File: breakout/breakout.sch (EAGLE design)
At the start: 140 parts, among them J15 1789472, J18 1789472, J29 69168-124HLF, J30 SJ1-3514-SMT-TR, J31 12226-8250-00FR, J32 1888276, J33 69168-116HLF, J34 1888276, J35 69168-116HLF, Q1 SI1012R, Q2 SI1012R, Q3 SI1012R, Q4 SI1012R, U1 G6K-2F-RF, U10 SN65LVDS9638DGN, U11 TINY-FPGA-BX, U2 G6K-2F-RF, U3 G6K-2F-RF, U4 G6K-2F-RF, U5 LTM4622A, U6 SI8610, U7 TCA9555, U8 FIN1032MTCX, U9 SN65LVDS9638DGN

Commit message: Added RGB LEDs and driver to breakout-board
- The old circuit, with single green LEDs driven by the TCA9555 is still
there and functional if this circuit is not populated
- If it is, the LED outputs on the TCA should be set to hiZ
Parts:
- removed D17, D18, D19, D20: (no value), jonnew:LED_3MM
- added C23: 0.1uF, jonnew:C_0402
- added C24: 10uF, jonnew:C_0805
- added D21, D22, D23, D24: (no value), jonnew:LED-RGB_5MM-THRU
- added R29, R30, R31, R32: 100, jonnew:R_0402
- added TP8, TP9: (no value), jonnew:TP_2MM
- added U12: (no value), jonnew:PCA9685_TSSOP
- D1, D2, D3, D4: device jonnew:DIODES1B-13-F -> jonnew:DIODE_S1B-13-F
- D15: device jonnew:Z-DIODE_DO214 -> jonnew:TVS-DIODE-BI_DO214
- R12, R13, R14: value 10k -> 4.7k
- R19, R20, R23, R24, R25, R26, R27, R28: value 1k -> 100
- R9: value 13.3k -> 12.5k
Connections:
- removed net N$10: D18.A, R16.2
- removed net N$11: D19.A, R17.2
- removed net N$2: D20.A, R18.2
- new net N$13: D22.CB, R25.1
- new net N$14: D22.CR, R24.1
- new net N$20: R25.2, U12.LED4
- new net N$21: R26.2, U12.LED5
- new net N$41: R24.2, U12.LED3
- new net N$42: D24.CG, R17.1, R29.1
- new net N$49: D23.CG, R16.1, R31.1
- new net N$50: D24.CB, R27.1
- new net N$51: R19.2, U12.LED2
- new net N$52: D24.CR, R28.1
- new net N$53: D23.CB, R30.1
- new net N$54: R23.2, U12.LED1
- new net N$55: D23.CR, R32.1
- new net N$56: R27.2, U12.LED10
- new net N$57: R29.2, U12.LED8
- new net N$58: R28.2, U12.LED9
- new net N$59: R30.2, U12.LED12
- new net N$6: D21.CG, R18.1, R19.1
- new net N$60: R31.2, U12.LED13
- new net N$61: R32.2, U12.LED11
- new net N$7: D21.CB, R20.1
- new net N$8: D21.CR, R23.1
- new net N$9: R20.2, U12.LED0
- net +3V3: now also C23.2, C24.2, D21.A, D22.A, D23.A, D24.A, U12.VCC; no longer R15.1, R16.1, R17.1, R18.1, S10.P, S11.P, S12.P, S5.P, S6.P, S7.P, S8.P, S9.P
- net AGND: now also D15.1, J18.1, J18.2; no longer D15.A, J18.7, J18.8
- net AIO_10: now also D15.2, J18.7; no longer D15.C, J18.5
- net AIO_11: now also J18.8; no longer J18.6
- net AIO_6: now also J18.3; no longer J18.1
- net AIO_7: now also J18.4; no longer J18.2
- net AIO_8: now also J18.5; no longer J18.3
- net AIO_9: now also J18.6; no longer J18.4
- net BUTTON1: now also S5.P; no longer R19.1, S5.S
- net BUTTON2: now also S6.P; no longer R20.1, S6.S
- net BUTTON3: now also S7.P; no longer R23.1, S7.S
- net BUTTON4: now also S8.P; no longer R24.1, S8.S
- net BUTTON5: now also S9.P; no longer R25.1, S9.S
- net BUTTON6: now also S10.P; no longer R26.1, S10.S
- net BUTTON7: now also S11.P; no longer R27.1, S11.S
- net BUTTON8: now also S12.P; no longer R28.1, S12.S
- net DOUT0: now also J32.2; no longer J32.1
- net DOUT1: now also J32.3; no longer J32.2
- net DOUT2: now also J32.4; no longer J32.3
- net DOUT3: now also J32.5; no longer J32.4
- net DOUT4: now also J32.6; no longer J32.5
- net DOUT5: now also J32.7; no longer J32.6
- net DOUT6: now also J32.8; no longer J32.7
- net DOUT7: now also J32.9; no longer J32.8
- net GND: now also C23.1, C24.1, J32.1, S10.S, S11.S, S12.S, S5.S, S6.S, S7.S, S8.S, S9.S, TP8.TP, TP9.TP, U12.!OE, U12.A0, U12.A1, U12.A2, U12.A3, U12.A4, U12.A5, U12.EXTCLK, U12.VSS; no longer J32.9, R19.2, R20.2, R23.2, R24.2, R25.2, R26.2, R27.2, R28.2
- net I2C_SCL: now also U12.SCL
- net I2C_SDA: now also U12.SDA
- net LED1: now also R18.2; no longer D20.C
- net LED2: now also R15.2; no longer D17.C
- net LED3: now also R17.2, U7.P06; no longer D19.C, U7.P07
- net LED4: now also R16.2, U7.P07; no longer D18.C, U7.P06
- net N$12: now also D22.CG, R15.1, R26.1; no longer D17.A, R15.2
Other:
- note added: "ADDR: 0100000X"
- note added: "ADDR: 1000000X"
- note added: "NB: This is actually 3.5V to get the most out of RGB driver."
- note added: "RGB LEDs"
- moved on the sheet: C16, J33, R12, R13, R14, R15, R16, R17, R18, R19, R20, R23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

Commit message: Updates to breakout revision 1.3 during testing
- Added input protection to digital IO after blowin up my FPGA during
testing
- Moved analog TVS diodes to top side to reduce manufacturing costs
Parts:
- removed S11, S12: CHERRY-MX, jonnew:SPST_TACT2_CHERRY-MX
- added D17, D18, D19, D20: WP154A4SEJ3VBDZGW/CA, jonnew:LED-RGB_5MM-THRU
- added D25, D34: CM1213−08MR, jonnew:TVS-DIODE-BI-8_MSOP
- added D26, D27, D28, D29, D30, D31, D32, D33, D35, D36, D37, D38: BAT54SLT1G, jonnew:DIODE2_SOT23
- added R33: 100, jonnew:R_0402
- added R34, R35, R36, R37, R38, R39, R40, R41, R42, R43, R44, R45, R46, R47, R48, R49: 270, 0.5W, jonnew:R_0805
- C17: value 4.7nF -> 10uF; device jonnew:C_0402 -> jonnew:C_0805
- C23: value 0.1uF -> 4.7nF
- C24: value 10uF -> 0.1uF; device jonnew:C_0805 -> jonnew:C_0402
- D21, D22, D23, D24: value (none) -> BAT54SLT1G; device jonnew:LED-RGB_5MM-THRU -> jonnew:DIODE2_SOT23
- J16: value (none) -> 1789472; device jonnew:COAX_MMCX-THRU -> jonnew:SCREW8_2
- J17, J28: device jonnew:COAX_SMA-VERT -> jonnew:COAX_MMCX-THRU
- J18: value 1789472 -> (none); device jonnew:SCREW8_2 -> jonnew:COAX_SMA-VERT
- J27: value (none) -> 69168-124HLF; device jonnew:COAX_MMCX-THRU -> jonnew:PINHD-2X12_0.1"
- J29: value 69168-124HLF -> (none); device jonnew:PINHD-2X12_0.1" -> jonnew:COAX_SMA-VERT
- J31: value 12226-8250-00FR -> 69168-116HLF; device jonnew:PINHD-1X26_122 -> jonnew:PINHD-2X8_THRU
- J32: value 1888276 -> 12226-8250-00FR; device jonnew:PINHD-1X9_SCREW2 -> jonnew:PINHD-1X26_122
- J33, J35: value 69168-116HLF -> 1888276; device jonnew:PINHD-2X8_THRU -> jonnew:PINHD-1X9_SCREW2
- J34: value 1888276 -> 69168-116HLF; device jonnew:PINHD-1X9_SCREW2 -> jonnew:PINHD-2X8_THRU
- R12, R13: value 4.7k -> 100
- R14: value 4.7k -> 1k
- R15, R17, R18: value 1k -> 100
- R16: value 1k -> 4.7k
- R19, R20, R21: value 100 -> 4.7k
- R22, R26, R31: value 100 -> 1k
- TP7: device jonnew:TPTP19R -> jonnew:TP_2MM
- TP9: device jonnew:TP_2MM -> jonnew:TPTP19R
- U10: value SN65LVDS9638DGN -> FIN1032MTCX; device jonnew:LVDS_DRIVER_DUAL_MSOP -> jonnew:LVDS_RECEIVER_QUAD_TSSOP
- U11: value TINY-FPGA-BX -> SN65LVDS9638DGN; device jonnew:TINY-FPGA-BX_BASIC -> jonnew:LVDS_DRIVER_DUAL_MSOP
- U12: value (none) -> SN65LVDS9638DGN; device jonnew:PCA9685_TSSOP -> jonnew:LVDS_DRIVER_DUAL_MSOP
- U7: value TCA9555 -> PCA9685; device jonnew:TCA9555 -> jonnew:PCA9685_TSSOP
- U8: value FIN1032MTCX -> TCA9555; device jonnew:LVDS_RECEIVER_QUAD_TSSOP -> jonnew:TCA9555
- U9: value SN65LVDS9638DGN -> TINY-FPGA-BX; device jonnew:LVDS_DRIVER_DUAL_MSOP -> jonnew:TINY-FPGA-BX_BASIC
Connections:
- removed net BUTTON1: S5.P, U7.P08
- removed net BUTTON2: S6.P, U7.P10
- new net !PCA9685_OE: R16.2, U7.!OE, U8.P08
- new net DIN0_P: D38.COMM, R49.1, U9.14
- new net DIN1_P: D29.COMM, R41.1, U9.15
- new net DIN2_P: D36.COMM, R47.1, U9.16/GBIN2
- new net DIN3_P: D27.COMM, R39.1, U9.9/10B
- new net DIN4_P: D33.COMM, R45.1, U9.10/26A
- new net DIN5_P: D24.COMM, R37.1, U9.11
- new net DIN6_P: D31.COMM, R43.1, U9.12
- new net DIN7_P: D22.COMM, R35.1, U9.13/26B
- new net DOUT0_P: D21.COMM, R34.1, U9.8
- new net DOUT1_P: D23.COMM, R36.1, U9.7/10A
- new net DOUT2_P: D26.COMM, R38.1, U9.6
- new net DOUT3_P: D28.COMM, R40.1, U9.5/3B
- new net DOUT4_P: D30.COMM, R42.1, U9.4
- new net DOUT5_P: D32.COMM, R44.1, U9.3/3A
- new net DOUT6_P: D35.COMM, R46.1, U9.2
- new net DOUT7_P: D37.COMM, R48.1, U9.1
- net !TCA_INT: now also R19.2, U8._INT; no longer R12.2, U7._INT
- net +12V: now also J32.1, J32.26, TP9.TP; no longer J31.1, J31.26, TP7.TP
- net +3V3: now also C17.2, C18.2, C23.1, C24.1, D17.A, D18.A, D19.A, D20.A, D21.C, D22.C, D23.C, D24.C, D25.VCC, D26.C, D27.C, D28.C, D29.C, D30.C, D31.C, D32.C, D33.C, D34.VCC, D35.C, D36.C, D37.C, D38.C, R16.1, R19.1, R20.1, R21.1, U10.EN, U11.VCC; no longer C17.1, C18.1, C23.2, C24.2, D21.A, D22.A, D23.A, D24.A, R12.1, R13.1, R14.1, U8.EN, U9.VCC
- net +5V0: now also U9.VIN; no longer U11.VIN
- net AGND: now also J16.1, J16.2, J27.1, J27.11, J27.13, J27.15, J27.17, J27.19, J27.21, J27.23, J27.3, J27.5, J27.7, J27.9, J32.13, J32.14, TP7.TP, TP8.TP; no longer J18.1, J18.2, J29.1, J29.11, J29.13, J29.15, J29.17, J29.19, J29.21, J29.23, J29.3, J29.5, J29.7, J29.9, J31.13, J31.14, TP5.TP, TP6.TP
- net AIO_0: now also J27.24, J32.20; no longer J29.24, J31.20
- net AIO_1: now also J27.22, J32.7; no longer J29.22, J31.7
- net AIO_10: now also J16.7, J27.4, J32.15; no longer J18.7, J29.4, J31.15
- net AIO_11: now also J16.8, J27.2, J32.2; no longer J18.8, J29.2, J31.2
- net AIO_2: now also J27.20, J32.19; no longer J29.20, J31.19
- net AIO_3: now also J27.18, J32.6; no longer J29.18, J31.6
- net AIO_4: now also J27.16, J32.18; no longer J29.16, J31.18
- net AIO_5: now also J27.14, J32.5; no longer J29.14, J31.5
- net AIO_6: now also J16.3, J27.12, J32.17; no longer J18.3, J29.12, J31.17
- net AIO_7: now also J16.4, J27.10, J32.4; no longer J18.4, J29.10, J31.4
- net AIO_8: now also J16.5, J27.8, J32.16; no longer J18.5, J29.8, J31.16
- net AIO_9: now also J16.6, J27.6, J32.3; no longer J18.6, J29.6, J31.3
- net BUTTON3: now also S5.P, U8.P05; no longer S7.P, U7.P05
- net BUTTON4: now also S6.P, U8.P11; no longer S8.P, U7.P11
- net BUTTON5: now also S7.P, U8.P09; no longer S9.P, U7.P09
- net BUTTON6: now also S8.P, U8.P12; no longer S10.P, U7.P12
- net BUTTON7: now also S9.P, U8.P04; no longer S11.P, U7.P04
- net BUTTON8: now also S10.P, U8.P13; no longer S12.P, U7.P13
- net DIN0: now also D34.CH4, R49.2; no longer U11.14
- net DIN1: now also D34.CH3, J34.4, J35.3, R41.2; no longer J34.3, J35.4, U11.15
- net DIN2: now also D34.CH2, J34.6, J35.4, R47.2; no longer J34.4, J35.6, U11.16/GBIN2
- net DIN3: now also D34.CH1, J34.8, J35.5, R39.2; no longer J34.5, J35.8, U11.9/10B
- net DIN4: now also D34.CH8, J34.10, J35.6, R45.2; no longer J34.6, J35.10, U11.10/26A
- net DIN5: now also D34.CH7, J34.12, J35.7, R37.2; no longer J34.7, J35.12, U11.11
- net DIN6: now also D34.CH6, J34.14, J35.8, R43.2; no longer J34.8, J35.14, U11.12
- net DIN7: now also D34.CH5, J34.16, J35.9, R35.2; no longer J34.9, J35.16, U11.13/26B
- net DOUT0: now also D25.CH8, J31.2, R34.2; no longer J32.2, U11.8
- net DOUT1: now also D25.CH7, J31.4, J33.3, R36.2; no longer J32.3, J33.4, U11.7/10A
- net DOUT2: now also D25.CH2, J31.6, J33.4, R38.2; no longer J32.4, J33.6, U11.6
- net DOUT3: now also D25.CH6, J31.8, J33.5, R40.2; no longer J32.5, J33.8, U11.5/3B
- net DOUT4: now also D25.CH3, J31.10, J33.6, R42.2; no longer J32.6, J33.10, U11.4
- net DOUT5: now also D25.CH5, J31.12, J33.7, R44.2; no longer J32.7, J33.12, U11.3/3A
- net DOUT6: now also D25.CH4, J31.14, J33.8, R46.2; no longer J32.8, J33.14, U11.2
- net DOUT7: now also D25.CH1, J31.16, J33.9, R48.2; no longer J32.9, J33.16, U11.1
- net GND: now also C17.1, C18.1, C23.2, C24.2, D21.A, D22.A, D23.A, D24.A, D25.VSS, D26.A, D27.A, D28.A, D29.A, D30.A, D31.A, D32.A, D33.A, D34.VSS, D35.A, D36.A, D37.A, D38.A, J18.2, J29.2, J31.1, J31.11, J31.13, J31.15, J31.3, J31.5, J31.7, J31.9, J32.PAD1, J32.PAD2, J34.11, J34.13, J34.15, J34.3, J34.5, J34.7, J34.9, TP5.TP, TP6.TP, U10.!EN, U10.C+, U10.C-, U10.D+, U10.D-, U12.BIN, U12.GND, U7.A3, U7.A4, U7.A5, U7.EXTCLK, U7.VSS, U8.A0, U8.A1, U8.A2; no longer C17.2, C18.2, C23.1, C24.1, J16.2, J27.2, J31.PAD1, J31.PAD2, J32.1, J33.11, J33.13, J33.15, J33.3, J33.5, J33.7, J33.9, J35.11, J35.13, J35.15, J35.3, J35.5, J35.7, J35.9, S11.S, S12.S, TP8.TP, TP9.TP, U10.BIN, U12.!OE, U12.A0, U12.A1, U12.A2, U12.A3, U12.A4, U12.A5, U12.EXTCLK, U12.VSS, U7.GND, U8.!EN, U8.C+, U8.C-, U8.D+, U8.D-
- net HARP_CLKOUT: now also U9.24; no longer U11.24
- net I2C_SCL: now also R20.2, U8.SCL, U9.23; no longer R13.2, U11.23, U12.SCL
- net I2C_SDA: now also R21.2, U8.SDA, U9.22; no longer R14.2, U11.22, U12.SDA
- net LED1: now also R14.2, U8.P14; no longer R18.2, U7.P14
- net LED2: now also R22.2, U8.P03; no longer R15.2, U7.P03
- net LED3: now also R26.2, U8.P06; no longer R17.2, U7.P06
- net LED4: now also R31.2, U8.P07; no longer R16.2, U7.P07
- net LVDS_DIN0_N: now also J32.23, U11.BOUT-; no longer J31.23, U9.BOUT-
- net LVDS_DIN0_P: now also J32.10, U11.BOUT+; no longer J31.10, U9.BOUT+
- net LVDS_DIN1_N: now also J32.11, U11.AOUT-; no longer J31.11, U9.AOUT-
- net LVDS_DIN1_P: now also J32.24, U11.AOUT+; no longer J31.24, U9.AOUT+
- net LVDS_DIN2_N: now also J32.25, U12.AOUT-; no longer J31.25, U10.AOUT-
- net LVDS_DIN2_P: now also J32.12, U12.AOUT+; no longer J31.12, U10.AOUT+
- net LVDS_DOUT0_N: now also J32.8, R29.1, U10.A-; no longer J31.8, R21.1, U8.A-
- net LVDS_DOUT0_P: now also J32.21, R29.2, U10.A+; no longer J31.21, R21.2, U8.A+
- net LVDS_DOUT1_N: now also J32.9, R32.1, U10.B-; no longer J31.9, R22.1, U8.B-
- net LVDS_DOUT1_P: now also J32.22, R32.2, U10.B+; no longer J31.22, R22.2, U8.B+
- net LVDS_IN_0: now also U10.AOUT, U9.18; no longer U11.18, U8.AOUT
- net LVDS_IN_1: now also U10.BOUT, U9.17; no longer U11.17, U8.BOUT
- net LVDS_OUT_0: now also U11.BIN, U9.19; no longer U11.19, U9.BIN
- net LVDS_OUT_1: now also U11.AIN, U9.20; no longer U11.20, U9.AIN
- net LVDS_OUT_2: now also U12.AIN, U9.21; no longer U10.AIN, U11.21
- net N$1: now also J18.1; no longer J16.1
- net N$12: now also D18.CG, R18.1, R22.1; no longer D22.CG, R15.1, R26.1
- net N$13: now also D18.CB, R17.1; no longer D22.CB, R25.1
- net N$14: now also D18.CR, R23.1; no longer D22.CR, R24.1
- net N$20: now also R17.2, U7.LED4; no longer R25.2, U12.LED4
- net N$21: now also R18.2, U7.LED5; no longer R26.2, U12.LED5
- net N$4: now also J29.1; no longer J27.1
- net N$41: now also R23.2, U7.LED3; no longer R24.2, U12.LED3
- net N$42: now also D19.CG, R25.1, R26.1; no longer D24.CG, R17.1, R29.1
- net N$49: now also D20.CG, R30.1; no longer D23.CG, R16.1
- net N$50: now also D19.CB, R24.1; no longer D24.CB, R27.1
- net N$51: now also R13.2, U7.LED2; no longer R19.2, U12.LED2
- net N$52: now also D19.CR, R27.1; no longer D24.CR, R28.1
- net N$53: now also D20.CB, R28.1; no longer D23.CB, R30.1
- net N$54: now also R15.2, U7.LED1; no longer R23.2, U12.LED1
- net N$55: now also D20.CR, R33.1; no longer D23.CR, R32.1
- net N$56: now also R24.2, U7.LED10; no longer R27.2, U12.LED10
- net N$57: now also R25.2, U7.LED8; no longer R29.2, U12.LED8
- net N$58: now also R27.2, U7.LED9; no longer R28.2, U12.LED9
- net N$59: now also R28.2, U7.LED12; no longer R30.2, U12.LED12
- net N$6: now also D17.CG, R13.1, R14.1; no longer D21.CG, R18.1, R19.1
- net N$60: now also R30.2, U7.LED13; no longer R31.2, U12.LED13
- net N$61: now also R33.2, U7.LED11; no longer R32.2, U12.LED11
- net N$7: now also D17.CB, R12.1; no longer D21.CB, R20.1
- net N$8: now also D17.CR, R15.1; no longer D21.CR, R23.1
- net N$9: now also R12.2, U7.LED0; no longer R20.2, U12.LED0
- net RELAY_SENSE_1: now also U8.P02; no longer U7.P02
- net RELAY_SENSE_2: now also U8.P01; no longer U7.P01
- net RELAY_SENSE_3: now also U8.P00; no longer U7.P00
- net RELAY_SENSE_4: now also U8.P15; no longer U7.P15
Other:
- note added: "NB: Assuming ~20pF combined parasitic capacitance of input proection and leads, fc = 1/(2*pi*270*20e-12) ~ 39MHz"
- moved on the sheet: C10, C11, C12, C13, C14, C15, C16, C17, C18, C19, C20, C21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

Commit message: Replaced RGB LED driver with neopixels
- This way we can have all kinds of status indicators on the board
- I added 41 of the 1.5x1.5mm neopixels for indicating power, harp, pll
lock, digital in, digital out, and analog IO state
- The control signal for these is going to have to come from one of the
SMD pads on the bottom of the TinyFPGA Bx. I just put a general purpose
jumper pad in there so that soder wire or 0.1" connector to wire can be
used instead of having a full connector under the FPGA board for a
single wire.
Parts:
- removed D35, D36, D37, D38: BAT54SLT1G, jonnew:DIODE2_SOT23
- removed R35, R36, R37, R38, R39, R40, R41, R42, R43, R44, R45, R46, R47, R48, R49: 270, 0.5W, jonnew:R_0805
- removed TP9: (no value), jonnew:TPTP19R
- added C25, C26, C27, C38, C39, C41, C42, C43, C45, C47, C49: 0.1uF, jonnew:C_0402
- added C28, C29, C30, C31, C40: 10uF, jonnew:C_0805
- added C32, C33, C34, C35: 47nF, jonnew:C_0402
- added C36, C37: 47uF, jonnew:C_1210
- added C44, C46, C48: 4.7nF, jonnew:C_0402
- added J36: 1888276, jonnew:PINHD-1X9_SCREW2
- added U13, U14, U15, U16, U17, U18, U19, U20, U21, U22, U23, U24, U25, U26, U27, U28, U29, U30, U31, U32, U33, U34, U35, U36, U37, U38, U39, U40, U41, U42: SK6805-E-J, jonnew:NEOPIXEL_1.5X1.5
- added U43, U44, U45, U46: G6K-2F-RF, jonnew:G6KU-2F-RF-TR09DC5
- added U47: LTM4622A, jonnew:LTM4622_BGA
- added U48: SI8610, CNP-ics 2:SI8610
- added U49: TINY-FPGA-BX, jonnew:TINY-FPGA-BX_BASIC
- added U50: TCA9555, jonnew:TCA9555
- added U51: FIN1032MTCX, jonnew:LVDS_RECEIVER_QUAD_TSSOP
- added U52, U53: SN65LVDS9638DGN, jonnew:LVDS_DRIVER_DUAL_MSOP
- C1, C13, C17, C2, C3, C4: value 10uF -> 0.1uF; device jonnew:C_0805 -> jonnew:C_0402
- C10, C9: value 47uF -> 0.1uF; device jonnew:C_1210 -> jonnew:C_0402
- C19, C23: value 4.7nF -> 0.1uF
- C21: value 4.7nF -> 47uF; device jonnew:C_0402 -> jonnew:C_1210
- C5, C6, C7: value 47nF -> 0.1uF
- C8: value 47nF -> 47uF; device jonnew:C_0402 -> jonnew:C_1210
- D17, D18, D19, D20: value WP154A4SEJ3VBDZGW/CA -> BAT54SLT1G; device jonnew:LED-RGB_5MM-THRU -> jonnew:DIODE2_SOT23
- D21, D30: value BAT54SLT1G -> CM1213−08MR; device jonnew:DIODE2_SOT23 -> jonnew:TVS-DIODE-BI-8_MSOP
- D25, D34: value CM1213−08MR -> BAT54SLT1G; device jonnew:TVS-DIODE-BI-8_MSOP -> jonnew:DIODE2_SOT23
- J31: value 69168-116HLF -> (none); device jonnew:PINHD-2X8_THRU -> jonnew:JP2E_THRU-HOLE
- J32: value 12226-8250-00FR -> 69168-116HLF; device jonnew:PINHD-1X26_122 -> jonnew:PINHD-2X8_THRU
- J33: value 1888276 -> 12226-8250-00FR; device jonnew:PINHD-1X9_SCREW2 -> jonnew:PINHD-1X26_122
- J34: value 69168-116HLF -> 1888276; device jonnew:PINHD-2X8_THRU -> jonnew:PINHD-1X9_SCREW2
- J35: value 1888276 -> 69168-116HLF; device jonnew:PINHD-1X9_SCREW2 -> jonnew:PINHD-2X8_THRU
- R1: value 1k -> 500
- R10: value 649k -> 49.9
- R11: value 8.25k -> 12.5k
- R12: value 100 -> 649k
- R13: value 100 -> 8.25k
- R14, R2: value 1k -> 4.7k
- R15: value 100 -> 4.7k
- R19, R20, R21: value 4.7k -> 270, 0.5W; device jonnew:R_0402 -> jonnew:R_0805
- R22, R26, R31: value 1k -> 270, 0.5W; device jonnew:R_0402 -> jonnew:R_0805
- R23, R24, R25, R27, R28, R29, R30, R32, R33: value 100 -> 270, 0.5W; device jonnew:R_0402 -> jonnew:R_0805
- R5, R6: value 49.9 -> 1k
- R9: value 12.5k -> 49.9
- TP8: device jonnew:TP_2MM -> jonnew:TPTP19R
- U1, U2, U3, U4: value G6K-2F-RF -> SK6805-E-J; device jonnew:G6KU-2F-RF-TR09DC5 -> jonnew:NEOPIXEL_1.5X1.5
- U10: value FIN1032MTCX -> (none); device jonnew:LVDS_RECEIVER_QUAD_TSSOP -> jonnew:LEVEL_SHIFTER_SOT23
- U11, U12: value SN65LVDS9638DGN -> SK6805-E-J; device jonnew:LVDS_DRIVER_DUAL_MSOP -> jonnew:NEOPIXEL_1.5X1.5
- U5: value LTM4622A -> SK6805-E-J; device jonnew:LTM4622_BGA -> jonnew:NEOPIXEL_1.5X1.5
- U6: value SI8610 -> SK6805-E-J; device CNP-ics 2:SI8610 -> jonnew:NEOPIXEL_1.5X1.5
- U7: value PCA9685 -> SK6805-E-J; device jonnew:PCA9685_TSSOP -> jonnew:NEOPIXEL_1.5X1.5
- U8: value TCA9555 -> SK6805-E-J; device jonnew:TCA9555 -> jonnew:NEOPIXEL_1.5X1.5
- U9: value TINY-FPGA-BX -> SK6805-E-J; device jonnew:TINY-FPGA-BX_BASIC -> jonnew:NEOPIXEL_1.5X1.5
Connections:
- removed net !PCA9685_OE: R16.2, U7.!OE, U8.P08
- removed net BUTTON6: S8.P, U8.P12
- removed net BUTTON7: S9.P, U8.P04
- removed net BUTTON8: S10.P, U8.P13
- removed net LED1: R14.2, U8.P14
- removed net LED2: R22.2, U8.P03
- removed net LED3: R26.2, U8.P06
- removed net LED4: R31.2, U8.P07
- removed net N$12: D18.CG, R18.1, R22.1
- removed net N$50: D19.CB, R24.1
- removed net N$59: R28.2, U7.LED12
- removed net N$6: D17.CG, R13.1, R14.1
- removed net N$60: R30.2, U7.LED13
- removed net N$61: R33.2, U7.LED11
- removed net RELAY_SENSE_4: C4.2, Q4.G, R4.1, U8.P15
- new net BUTTON0: S6.P, U50.P11
- new net BUTTON1: S5.P, U50.P05
- new net BUTTON2: S8.P, U50.P12
- new net LOCKED: U11.DIN, U9.DOUT
- new net N$10: U36.DOUT, U37.DIN
- new net N$11: U31.DOUT, U32.DIN
- new net N$62: U32.DOUT, U33.DIN
- new net N$63: U33.DOUT, U34.DIN
- new net N$64: U34.DOUT, U35.DIN
- new net N$65: U35.DOUT, U36.DIN
- new net N$67: U37.DOUT, U38.DIN
- new net N$68: U38.DOUT, U39.DIN
- new net N$69: U39.DOUT, U40.DIN
- new net N$70: U40.DOUT, U41.DIN
- new net N$71: U41.DOUT, U42.DIN
- new net N$72: U18.DOUT, U19.DIN
- new net N$73: U19.DOUT, U20.DIN
- new net N$74: U20.DOUT, U21.DIN
- new net N$75: U21.DOUT, U22.DIN
- new net N$76: U22.DOUT, U23.DIN
- new net N$77: U23.DOUT, U24.DIN
- new net N$78: U24.DOUT, U25.DIN
- new net N$79: U25.DOUT, U26.DIN
- new net N$80: U26.DOUT, U27.DIN
- new net N$81: U27.DOUT, U28.DIN
- new net N$82: U28.DOUT, U29.DIN
- new net N$83: U29.DOUT, U30.DIN
- new net N$84: U30.DOUT, U31.DIN
- new net NEOPIXEL_DIN: J31.1, U10.A
- new net RELAY_SENSE_0: C28.2, Q1.G, R3.2, U50.P02
- net !TCA_INT: now also R14.2, U50._INT; no longer R19.2, U8._INT
- net +12V: now also C40.2, J33.1, J33.26, TP8.TP, U47.RUN1, U47.RUN2, U47.VIN; no longer C13.2, J32.1, J32.26, TP9.TP, U5.RUN1, U5.RUN2, U5.VIN
- net +3V3: now also C1.1, C37.2, C43.2, C44.1, C45.1, C46.1, C47.1, C48.1, C49.1, D17.C, D18.C, D19.C, D20.C, D21.VCC, D25.C, D30.VCC, D34.C, R14.1, R15.1, R2.1, U10.VCCA, U47.VOUT1, U50.VCC, U51.EN, U51.VCC, U52.VCC, U53.VCC; no longer C10.2, C16.2, C17.2, C18.2, C19.1, C20.1, C21.1, C22.1, C23.1, C24.1, D17.A, D18.A, D19.A, D20.A, D21.C, D25.VCC, D30.C, D34.VCC, D35.C, D36.C, D37.C, D38.C, R19.1, R20.1, R21.1, U10.EN, U10.VCC, U11.VCC, U12.VCC, U5.VOUT1, U7.VCC, U8.VCC
- net +5V0: now also C10.2, C11.2, C12.2, C13.2, C14.2, C16.2, C17.2, C18.2, C19.2, C2.1, C20.2, C21.2, C22.2, C23.2, C24.2, C25.2, C26.2, C27.2, C3.2, C36.2, C4.2, C42.2, C5.2, C6.2, C7.2, C8.2, U1.VDD, U10.VCCB, U11.VDD, U12.VDD, U13.VDD, U14.VDD, U15.VDD, U16.VDD, U17.VDD, U18.VDD, U19.VDD, U2.VDD, U20.VDD, U21.VDD, U22.VDD, U23.VDD, U24.VDD, U25.VDD, U26.VDD, U27.VDD, U28.VDD, U29.VDD, U3.VDD, U30.VDD, U31.VDD, U32.VDD, U33.VDD, U34.VDD, U35.VDD, U36.VDD, U37.VDD, U38.VDD, U39.VDD, U4.VDD, U40.VDD, U41.VDD, U42.VDD, U47.VOUT2, U48.AVDD, U49.VIN, U5.VDD, U6.VDD, U7.VDD, U8.VDD, U9.VDD; no longer U5.VOUT2, U6.AVDD, U9.VIN
- net AGND: now also J33.13, J33.14; no longer J32.13, J32.14, TP8.TP
- net AIO_0: now also J33.20; no longer J32.20
- net AIO_1: now also J33.7; no longer J32.7
- net AIO_10: now also J33.15; no longer J32.15
- net AIO_11: now also J33.2; no longer J32.2
- net AIO_2: now also J33.19; no longer J32.19
- net AIO_3: now also J33.6; no longer J32.6
- net AIO_4: now also J33.18; no longer J32.18
- net AIO_5: now also J33.5; no longer J32.5
- net AIO_6: now also J33.17; no longer J32.17
- net AIO_7: now also J33.4; no longer J32.4
- net AIO_8: now also J33.16; no longer J32.16
- net AIO_9: now also J33.3; no longer J32.3
- net BUTTON3: now also S7.P, U50.P09; no longer S5.P, U8.P05
- net BUTTON4: now also S10.P, U50.P13; no longer S6.P, U8.P11
- net BUTTON5: now also S9.P, U50.P04; no longer S7.P, U8.P09
- net DIN0: now also D30.CH4, J36.2, R34.2; no longer D34.CH4, J34.2, R49.2
- net DIN0_P: now also D34.COMM, R34.1, U49.14; no longer D38.COMM, R49.1, U9.14
- net DIN1: now also D30.CH3, J35.4, J36.3, R26.2; no longer D34.CH3, J34.4, J35.3, R41.2
- net DIN1_P: now also D25.COMM, R26.1, U49.15; no longer D29.COMM, R41.1, U9.15
- net DIN2: now also D30.CH2, J35.6, J36.4, R32.2; no longer D34.CH2, J34.6, J35.4, R47.2
- net DIN2_P: now also D32.COMM, R32.1, U49.16/GBIN2; no longer D36.COMM, R47.1, U9.16/GBIN2
- net DIN3: now also D30.CH1, J35.8, J36.5, R24.2; no longer D34.CH1, J34.8, J35.5, R39.2
- net DIN3_P: now also D23.COMM, R24.1, U49.9/10B; no longer D27.COMM, R39.1, U9.9/10B
- net DIN4: now also D30.CH8, J35.10, J36.6, R30.2; no longer D34.CH8, J34.10, J35.6, R45.2
- net DIN4_P: now also D29.COMM, R30.1, U49.10/26A; no longer D33.COMM, R45.1, U9.10/26A
- net DIN5: now also D30.CH7, J35.12, J36.7, R22.2; no longer D34.CH7, J34.12, J35.7, R37.2
- net DIN5_P: now also D20.COMM, R22.1, U49.11; no longer D24.COMM, R37.1, U9.11
- net DIN6: now also D30.CH6, J35.14, J36.8, R28.2; no longer D34.CH6, J34.14, J35.8, R43.2
- net DIN6_P: now also D27.COMM, R28.1, U49.12; no longer D31.COMM, R43.1, U9.12
- net DIN7: now also D30.CH5, J35.16, J36.9, R20.2; no longer D34.CH5, J34.16, J35.9, R35.2
- net DIN7_P: now also D18.COMM, R20.1, U49.13/26B; no longer D22.COMM, R35.1, U9.13/26B
- net DOUT0: now also D21.CH8, J32.2, J34.2, R19.2; no longer D25.CH8, J31.2, J33.2, R34.2
- net DOUT0_P: now also D17.COMM, R19.1, U49.8; no longer D21.COMM, R34.1, U9.8
- net DOUT1: now also D21.CH7, J32.4, J34.3, R21.2; no longer D25.CH7, J31.4, J33.3, R36.2
- net DOUT1_P: now also D19.COMM, R21.1, U49.7/10A; no longer D23.COMM, R36.1, U9.7/10A
- net DOUT2: now also D21.CH2, J32.6, J34.4, R23.2; no longer D25.CH2, J31.6, J33.4, R38.2
- net DOUT2_P: now also D22.COMM, R23.1, U49.6; no longer D26.COMM, R38.1, U9.6
- net DOUT3: now also D21.CH6, J32.8, J34.5, R25.2; no longer D25.CH6, J31.8, J33.5, R40.2
- net DOUT3_P: now also D24.COMM, R25.1, U49.5/3B; no longer D28.COMM, R40.1, U9.5/3B
- net DOUT4: now also D21.CH3, J32.10, J34.6, R27.2; no longer D25.CH3, J31.10, J33.6, R42.2
- net DOUT4_P: now also D26.COMM, R27.1, U49.4; no longer D30.COMM, R42.1, U9.4
- net DOUT5: now also D21.CH5, J32.12, J34.7, R29.2; no longer D25.CH5, J31.12, J33.7, R44.2
- net DOUT5_P: now also D28.COMM, R29.1, U49.3/3A; no longer D32.COMM, R44.1, U9.3/3A
- net DOUT6: now also D21.CH4, J32.14, J34.8, R31.2; no longer D25.CH4, J31.14, J33.8, R46.2
- net DOUT6_P: now also D31.COMM, R31.1, U49.2; no longer D35.COMM, R46.1, U9.2
- net DOUT7: now also D21.CH1, J32.16, J34.9, R33.2; no longer D25.CH1, J31.16, J33.9, R48.2
- net DOUT7_P: now also D33.COMM, R33.1, U49.1; no longer D37.COMM, R48.1, U9.1
- net GND: now also C1.2, C14.1, C19.1, C2.2, C20.1, C21.1, C22.1, C23.1, C24.1, C25.1, C26.1, C27.1, C28.1, C29.1, C30.1, C31.1, C36.1, C37.1, C38.1, C39.1, C40.1, C42.1, C43.1, C44.2, C45.2, C46.2, C47.2, C48.2, C49.2, C5.1, C6.1, C7.1, C8.1, D17.A, D18.A, D19.A, D20.A, D21.VSS, D25.A, D30.VSS, D34.A, J31.2, J32.1, J32.11, J32.13, J32.15, J32.3, J32.5, J32.7, J32.9, J33.PAD1, J33.PAD2, J35.11, J35.13, J35.15, J35.3, J35.5, J35.7, J35.9, J36.1, R12.2, R13.2, U1.GND, U13.GND, U14.GND, U15.GND, U16.GND, U17.GND, U18.GND, U19.GND, U2.GND, U20.GND, U21.GND, U22.GND, U23.GND, U24.GND, U25.GND, U26.GND, U27.GND, U28.GND, U29.GND, U3.GND, U30.GND, U31.GND, U32.GND, U33.GND, U34.GND, U35.GND, U36.GND, U37.GND, U38.GND, U39.GND, U4.GND, U40.GND, U41.GND, U42.GND, U43.CASE, U43.COIL-, U44.CASE, U44.COIL-, U45.CASE, U45.COIL-, U46.CASE, U46.COIL-, U47.GND, U47.SYNC/MODE, U48.AGND, U49.GND, U50.A0, U50.A1, U50.A2, U50.GND, U51.!EN, U51.C+, U51.C-, U51.D+, U51.D-, U51.GND, U52.GND, U53.BIN, U53.GND, U6.GND, U7.GND; no longer C1.1, C19.2, C2.1, C20.2, C21.2, C22.2, C23.2, C24.2, D21.A, D25.VSS, D30.A, D34.VSS, D35.A, D36.A, D37.A, D38.A, J31.1, J31.11, J31.13, J31.15, J31.3, J31.5, J31.7, J31.9, J32.PAD1, J32.PAD2, J33.1, J34.11, J34.13, J34.15, J34.3, J34.5, J34.7, J34.9, R5.2, R6.2, U1.CASE, U1.COIL-, U10.!EN, U10.C+, U10.C-, U10.D+, U10.D-, U12.BIN, U2.CASE, U2.COIL-, U3.CASE, U3.COIL-, U4.CASE, U4.COIL-, U5.SYNC/MODE, U6.AGND, U7.A0, U7.A1, U7.A2, U7.A3, U7.A4, U7.A5, U7.EXTCLK, U7.VSS, U8.A0, U8.A1, U8.A2
- net HARP_CLKOUT: now also U48.A1, U49.24; no longer U6.A1, U9.24
- net I2C_SCL: now also R15.2, U49.23, U50.SCL; no longer R20.2, U7.SCL, U8.SCL, U9.23
- net I2C_SDA: now also R16.2, U49.22, U50.SDA; no longer R21.2, U7.SDA, U8.SDA, U9.22
- net LVDS_DIN0_N: now also J33.23, U52.BOUT-; no longer J32.23, U11.BOUT-
- net LVDS_DIN0_P: now also J33.10, U52.BOUT+; no longer J32.10, U11.BOUT+
- net LVDS_DIN1_N: now also J33.11, U52.AOUT-; no longer J32.11, U11.AOUT-
- net LVDS_DIN1_P: now also J33.24, U52.AOUT+; no longer J32.24, U11.AOUT+
- net LVDS_DIN2_N: now also J33.25, U53.AOUT-; no longer J32.25, U12.AOUT-
- net LVDS_DIN2_P: now also J33.12, U53.AOUT+; no longer J32.12, U12.AOUT+
- net LVDS_DOUT0_N: now also J33.8, R17.1, U51.A-; no longer J32.8, R29.1, U10.A-
- net LVDS_DOUT0_P: now also J33.21, R17.2, U51.A+; no longer J32.21, R29.2, U10.A+
- net LVDS_DOUT1_N: now also J33.9, R18.1, U51.B-; no longer J32.9, R32.1, U10.B-
- net LVDS_DOUT1_P: now also J33.22, R18.2, U51.B+; no longer J32.22, R32.2, U10.B+
- net LVDS_IN_0: now also U49.18, U51.AOUT; no longer U10.AOUT, U9.18
- net LVDS_IN_1: now also U49.17, U51.BOUT; no longer U10.BOUT, U9.17
- net LVDS_OUT_0: now also U49.19, U52.BIN; no longer U11.BIN, U9.19
- net LVDS_OUT_1: now also U49.20, U52.AIN; no longer U11.AIN, U9.20
- net LVDS_OUT_2: now also U49.21, U53.AIN; no longer U12.AIN, U9.21
- net N$13: now also U15.DOUT, U16.DIN; no longer D18.CB, R17.1
- net N$14: now also U16.DOUT, U17.DIN; no longer D18.CR, R23.1
- net N$145: now also R12.1, U47.FREQ; no longer R10.1, U5.FREQ
- net N$15: now also C32.2, U43.NC_A; no longer C5.2, U1.NC_A
- net N$16: now also C41.1, U48.BVDD; no longer C14.1, U6.BVDD
- net N$17: now also C41.2, U48.BGND; no longer C14.2, U6.BGND
- net N$18: now also U48.B1; no longer U6.B1
- net N$19: now also U44.NO_A; no longer U2.NO_A
- net N$20: now also U17.DOUT, U18.DIN; no longer R17.2, U7.LED4
- net N$21: now also U1.DOUT, U2.DIN; no longer R18.2, U7.LED5
- net N$22: now also C33.1, R8.1; no longer C6.1, R6.1
- net N$23: now also R3.1; no longer R1.1
- net N$24: now also R13.1, U47.FB2; no longer R11.1, U5.FB2
- net N$25: now also R11.1, U47.FB1; no longer R9.1, U5.FB1
- net N$26: now also C38.2, U47.TRACK/SS2; no longer C11.2, U5.TRACK/SS2
- net N$27: now also C39.2, U47.TRACK/SS1; no longer C12.2, U5.TRACK/SS1
- net N$28: now also U43.NO_A; no longer U1.NO_A
- net N$29: now also U43.COM_A; no longer U1.COM_A
- net N$30: now also C32.1, R7.1; no longer C5.1, R5.1
- net N$31: now also C33.2, U44.NC_A; no longer C6.2, U2.NC_A
- net N$32: now also U45.COIL+; no longer U3.COIL+
- net N$33: now also C34.1, R9.1; no longer C7.1, R7.1
- net N$34: now also U44.COM_A; no longer U2.COM_A
- net N$35: now also R4.2; no longer R2.2
- net N$36: now also C34.2, U45.NC_A; no longer C7.2, U3.NC_A
- net N$37: now also U45.NO_A; no longer U3.NO_A
- net N$38: now also R5.2; no longer R3.2
- net N$39: now also U46.COIL+; no longer U4.COIL+
- net N$40: now also U44.COIL+; no longer U2.COIL+
- net N$41: now also U2.DOUT, U3.DIN; no longer R23.2, U7.LED3
- net N$42: now also U3.DOUT, U4.DIN; no longer D19.CG, R25.1, R26.1
- net N$43: now also U45.COM_A; no longer U3.COM_A
- net N$44: now also R6.2; no longer R4.2
- net N$45: now also C35.1, R10.1; no longer C8.1, R8.1
- net N$46: now also C35.2, U46.NC_A; no longer C8.2, U4.NC_A
- net N$47: now also U46.NO_A; no longer U4.NO_A
- net N$48: now also U46.COM_A; no longer U4.COM_A
- net N$49: now also U4.DOUT, U5.DIN; no longer D20.CG, R30.1, R31.1
- net N$5: now also U43.COIL+; no longer U1.COIL+
- net N$51: now also U6.DOUT, U7.DIN; no longer R13.2, U7.LED2
- net N$52: now also U7.DOUT, U8.DIN; no longer D19.CR, R27.1
- net N$53: now also U8.DOUT, U9.DIN; no longer D20.CB, R28.1
- net N$54: now also R1.2, U1.DIN; no longer R15.2, U7.LED1
- net N$55: now also R1.1, U10.B; no longer D20.CR, R33.1
- net N$56: now also U5.DOUT, U6.DIN; no longer R24.2, U7.LED10
- net N$57: now also R2.2, U10.OE; no longer R25.2, U7.LED8
- net N$58: now also U14.DOUT, U15.DIN; no longer R27.2, U7.LED9
- net N$7: now also U11.DOUT, U12.DIN; no longer D17.CB, R12.1
- net N$8: now also U12.DOUT, U13.DIN; no longer D17.CR, R15.1
- net N$9: now also U13.DOUT, U14.DIN; no longer R12.2, U7.LED0
- net RELAY_SENSE_1: now also C29.2, Q2.G, R4.1, U50.P01; no longer C1.2, Q1.G, R1.2, U8.P02
- net RELAY_SENSE_2: now also C30.2, Q3.G, R5.1, U50.P00; no longer C2.2, Q2.G, R2.1, U8.P01
- net RELAY_SENSE_3: now also C31.2, Q4.G, R6.1, U50.P15; no longer C3.2, Q3.G, R3.1, U8.P00
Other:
- note added: "A11"
- note added: "BUT0"
- note added: "BUT1"
- note added: "BUT2"
- note added: "BUT3"
- note added: "BUT4"
- note added: "BUT5"
- note added: "DI0"
- note added: "DI1"
- note added: "DI2"
- note added: "DI3"
- note added: "DI4"
- note added: "DI5"
- note added: "DI6"
- note added: "DI7"
- note added: "DO0"
- note added: "DO1"
- note added: "DO2"
- note added: "DO3"
- note added: "DO4"
- note added: "DO5"
- note added: "DO6"
- note added: "DO7"
- note added: "HARP"
- note added: "HS0"
- note added: "HS1"
- note added: "HS2"
- note added: "HS3"
- note added: "Jumper wire to pinxx on bottom of TinyFPGA"
- note added: "LOCK"
- note added: "PWR"
- note added: "Status LEDs"
- note removed: "ADDR: 1000000X"
- note removed: "RGB LEDs"
- moved on the sheet: C1, C10, C11, C12, C13, C14, C15, C16, C17, C18, C19, C2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

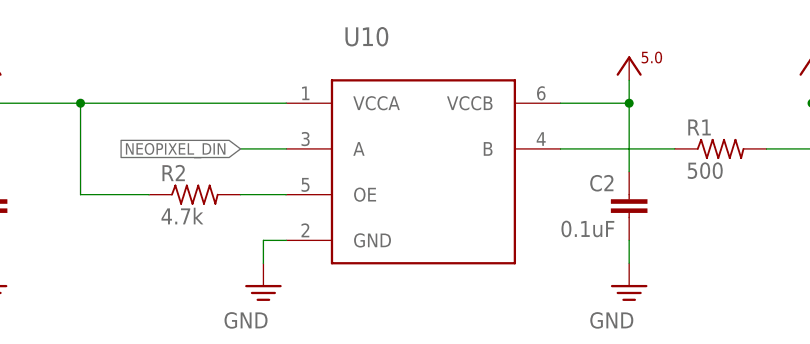
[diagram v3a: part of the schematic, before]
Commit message: Increased minimum hole size to 0.3 mm on breakout rev 1.3
- Ready for production
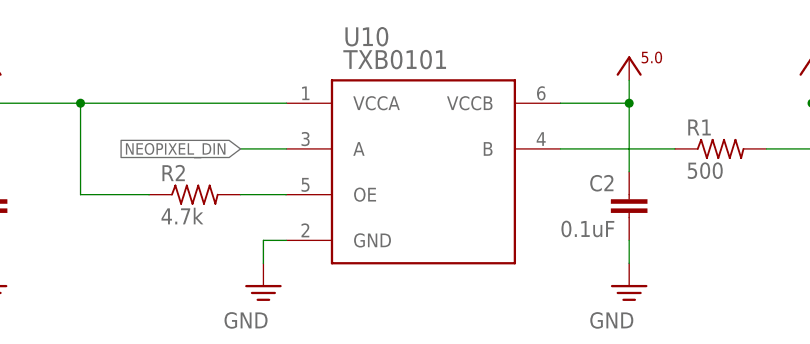
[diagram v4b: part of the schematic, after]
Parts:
- U10: value (none) -> TXB0101
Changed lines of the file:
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@@
 <clearance class="1" value="0.1"/>
 </class>
-<class number="3" name="100 Ohm Diff Mid" width="0.19" drill="0.2">
+<class number="3" name="100 Ohm Diff Mid" width="0.19" drill="0.3">
 <clearance class="3" value="0.09"/>
 </class>
@@
 <part name="J31" library="jonnew" deviceset="JP2E" device="_THRU-HOLE"/>
 <part name="SUPPLY120" library="jonnew" deviceset="GND" device=""/>
-<part name="U10" library="jonnew" deviceset="LEVEL_SHIFTER" device="_SOT23"/>
+<part name="U10" library="jonnew" deviceset="LEVEL_SHIFTER" device="_SOT23" value="TXB0101"/>
 <part name="C1" library="jonnew" deviceset="C" device="_0402" value="0.1uF"/>
 <part name="SUPPLY121" library="jonnew" deviceset="GND" device=""/>

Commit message: Initial commit of breakout rev 1.4
- Fixes to analog routing to maintain consistancy of analog and digital
pin ordering in the screw terminals and IDC headers
- Switch the ordering of BNC analog connector to row major and aligned
in column direction.
- Add a secondary, internally controlled FET in series with the coil on
each headstage relay so that certain ports can be disabled when
instructed from host.
- Changed the optical table mounting holes to slots that can accomidate
both metric and imperial spacing.
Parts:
- added Q5, Q6, Q7, Q8: SI1012R, jonnew:N-MOSFET_SC75-GSD
- added R35, R37, R39, R41: 100k, jonnew:R_0402
- added R36, R38, R40, R42: 1k, jonnew:R_0402
- R11: value 12.5k -> 13.3k
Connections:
- removed net N$39: D4.C, Q4.S, U46.COIL+
- removed net RELAY_SENSE_0: C28.2, Q1.G, R3.2, U50.P02
- removed net RELAY_SENSE_1: C29.2, Q2.G, R4.1, U50.P01
- removed net RELAY_SENSE_2: C30.2, Q3.G, R5.1, U50.P00
- removed net RELAY_SENSE_3: C31.2, Q4.G, R6.1, U50.P15
- new net N$12: D2.A, Q2.D, U44.COIL-
- new net N$50: D3.A, Q3.D, U45.COIL-
- new net N$59: D4.A, Q4.D, U46.COIL-
- new net N$6: Q1.S, Q5.D
- new net N$60: Q4.S, Q8.D
- new net RELAY_AND_0: Q5.G, R36.2, U50.P04
- new net RELAY_AND_1: Q6.G, R38.2, U50.P02
- new net RELAY_AND_2: Q7.G, R40.2, U50.P00
- new net RELAY_AND_3: Q8.G, R42.2, U50.P17
- new net RELAY_MECH_0: C28.2, Q1.G, R3.2, R35.2, U50.P05
- new net RELAY_MECH_1: C29.2, Q2.G, R37.2, R4.1, U50.P03
- new net RELAY_MECH_2: C30.2, Q3.G, R39.2, R5.1, U50.P01
- new net RELAY_MECH_3: C31.2, Q4.G, R41.2, R6.1, U50.P16
- net +5V0: now also D1.C, D2.C, D3.C, D4.C, U43.COIL+, U44.COIL+, U45.COIL+, U46.COIL+; no longer Q1.D, Q2.D, Q3.D, Q4.D
- net AIO_0: now also J27.2; no longer J27.24
- net AIO_1: now also J27.4; no longer J27.22
- net AIO_10: now also J27.22; no longer J27.4
- net AIO_11: now also J27.24; no longer J27.2
- net AIO_2: now also J27.6; no longer J27.20
- net AIO_3: now also J27.8; no longer J27.18
- net AIO_4: now also J27.10; no longer J27.16
- net AIO_5: now also J27.12; no longer J27.14
- net AIO_6: now also J27.14; no longer J27.12
- net AIO_7: now also J27.16; no longer J27.10
- net AIO_8: now also J27.18; no longer J27.8
- net AIO_9: now also J27.20; no longer J27.6
- net BUTTON0: now also U50.P13; no longer U50.P11
- net BUTTON1: now also S8.P, U50.P14; no longer S5.P, U50.P05
- net BUTTON2: now also S10.P, U50.P15; no longer S8.P, U50.P12
- net BUTTON3: now also S5.P, U50.P07; no longer S7.P, U50.P09
- net BUTTON4: now also S7.P, U50.P11; no longer S10.P, U50.P13
- net BUTTON5: now also U50.P06; no longer U50.P04
- net GND: now also Q5.S, Q6.S, Q7.S, Q8.S, R35.1, R36.1, R37.1, R38.1, R39.1, R40.1, R41.1, R42.1; no longer D1.A, D2.A, D3.A, D4.A, U43.COIL-, U44.COIL-, U45.COIL-, U46.COIL-
- net N$32: now also Q7.D; no longer D3.C, U45.COIL+
- net N$40: now also Q6.D; no longer D2.C, U44.COIL+
- net N$5: now also D1.A, Q1.D, U43.COIL-; no longer D1.C, Q1.S, U43.COIL+
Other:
- note added: "A0"
- note added: "A1"
- note added: "A10"
- note added: "A2"
- note added: "A3"
- note added: "A4"
- note added: "A5"
- note added: "A6"
- note added: "A7"
- note added: "A8"
- note added: "A9"
- note added: "HST0"
- note added: "HST1"
- note added: "HST2"
- note added: "HST3"
- note added: "HST4"
- note added: "HST5"
- note added: "NB: TCA pins are default high. 1k overrides"
- note removed: "BUT0"
- note removed: "BUT1"
- note removed: "BUT2"
- note removed: "BUT3"
- note removed: "BUT4"
- note removed: "BUT5"
- note removed: "NB: This is actually 3.5V to get the most out of RGB driver."
- moved on the sheet: C28, C29, C30, C31, C32, C33, C34, D1, D2, D3, D4, J1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
